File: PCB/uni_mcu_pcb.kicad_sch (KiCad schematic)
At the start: 66 parts, among them J1 USB_C_Receptacle_USB2.0, J2 Conn_01x02_Male, J3 Conn_02x08_Odd_Even, Q1 Q_NPN_BCE, Q2 Q_NPN_BCE, Q3 Q_NPN_BCE, Q4 Q_NPN_BCE, Q5 FDS6890A, Q6 FDS6890A, SW1 SW_DIP_x01, SW2 SW_DIP_x01, SW3 SW_DIP_x01, U1 CC56-12CGKWA, U2 CH330N, U3 USBLC6-2P6, U4 STM32F030K6Tx, U5 LD1117S33TR_SOT223, U6 STM32F030C8Tx, U7 W25Q32JVSS, Y1 Crystal

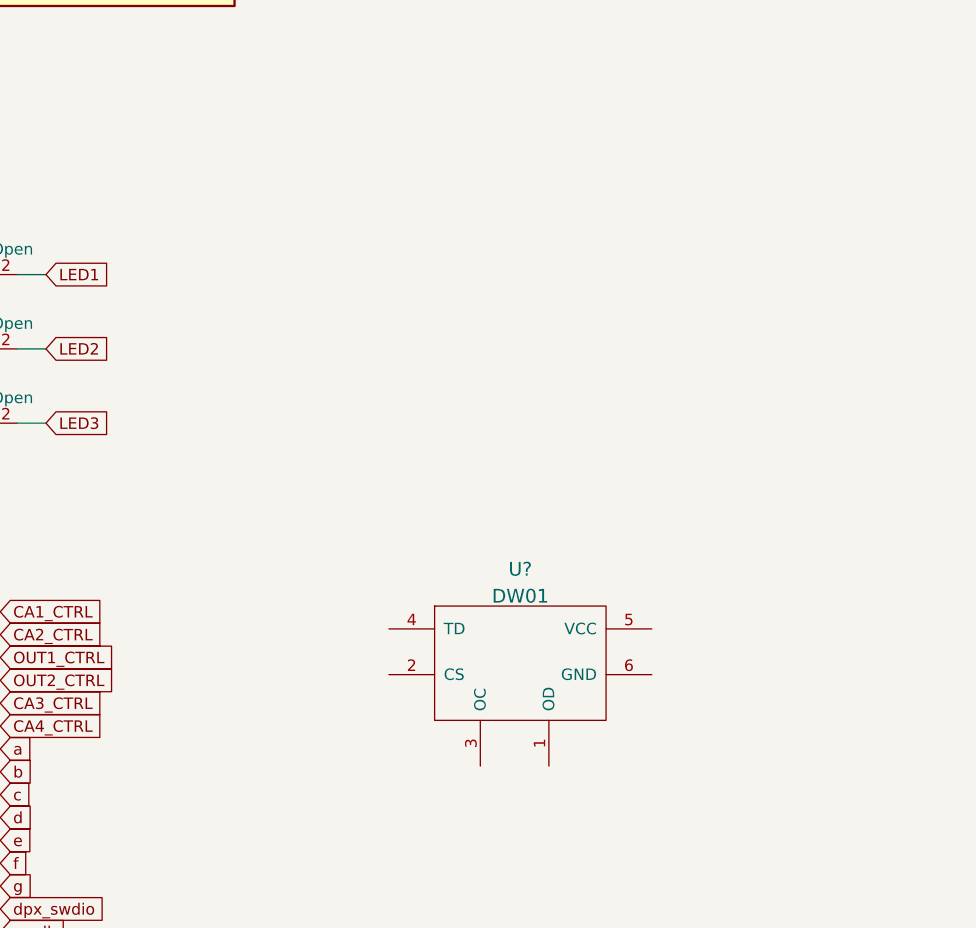
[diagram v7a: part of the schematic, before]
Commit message: Разводка модуля зарядки li-ion
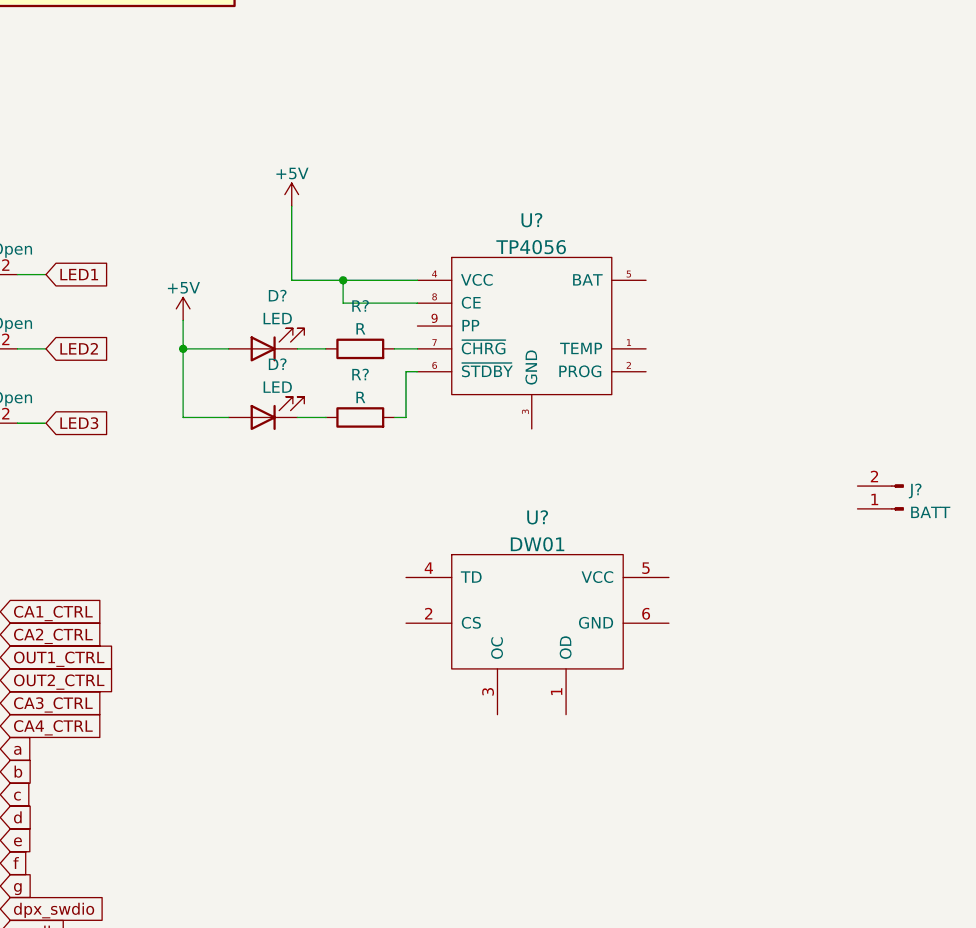
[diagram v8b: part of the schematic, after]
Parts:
- added D? (x2): LED, symbol Device:LED
- added J?: BATT, Connector_PinHeader_2.54mm:PinHeader_1x02_P2.54mm_Vertical, symbol Connector:Conn_01x02_Male
- added R? (x2): R, symbol Device:R
- added U?: TP4056, symbol mcuDebugBoard:TP4056
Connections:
- net +5V: now also D?.2 (A), D?.2 (A), U?.4 (VCC), U?.8 (CE)
- new net: D?.1 (K), R?.1 (x2)
- new net: R?.2, U?.6 (~{STDBY})
- new net: R?.2, U?.7 (~{CHRG})
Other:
- moved on the sheet: U?
